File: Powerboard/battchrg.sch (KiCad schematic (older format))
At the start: 48 parts, among them Q1(ACFET)? SI7617DN-T1-GE3

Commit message: 01022022
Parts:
- C14, C6: renamed from C?; value C_Small -> 0.1µF
- C15: renamed from C?; value ? -> 0.1µF
- C16: renamed from C?; value 2.2 μF -> 2.2μF
- C7: renamed from C?; value 1μF -> 1µF
- CTTC: renamed from CTTC?; value CP_Small -> 0.022µF
- L1: renamed from L?; value L -> 6.8µH
- R14, R15: renamed from R?; value R_Small -> 100kΩ
- R17: renamed from R?; value R_Small -> 10Ω
- R18: renamed from R?; value R_Small -> 1kΩ
- R4: renamed from R?; value R -> 150kΩ
- R6: renamed from R?; value R -> 13kΩ
- R8: renamed from R?; value R -> 32kΩ
- RAC: renamed from RAC?; value 0.010 -> 10mΩ
- RSR: renamed from RSR?; value 0.010 -> 10mΩ
- gave numbers to parts that had none: 28
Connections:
- net VDD is gone; now on net System: C15.1, C3.2, C8.1, C9.1, IC?.1 (ACN), Q3.5 (D_1), Q3.6 (D_2), Q3.7 (D_3), Q3.8 (D_4), Q4.5 (D_1), Q4.6 (D_2), Q4.7 (D_3), Q4.8 (D_4), R15.2, RAC.1
- net CE: now also R3.1, R5.1, R7.1, R9.2
- net GND: now also EXTPower.2 (Pin_2), J1.2 (Pin_2)
- net at J1.1 (Pin_1), R10.2, R16.2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: no longer J1.2 (Pin_2)
- net Stat1: now reaches IC?.5 (STAT1)
- net PG: now reaches IC?.8 (~PG)
- net Stat2: now reaches IC?.9 (STAT2)
- net at EXTPower.1 (Pin_1), Q1(ACFET).1 (S_1), Q1(ACFET).2 (S_2)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: no longer EXTPower.2 (Pin_2)
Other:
- moved on the sheet: C15, C4, J1, R15, R9

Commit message: 08/02/2022 update3
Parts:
- added MainPowerDiode: LED, symbol Device:LED
- added MainPowerSwitch: Conn_01x02_Female, symbol Connector:Conn_01x02_Female
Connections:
- net at Q1(ACFET).1 (S_1), Q1(ACFET).2 (S_2), Q1(ACFET).3 (S_3)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: now also MainPowerDiode.1 (K); no longer EXTPower.1 (Pin_1)
- new net: EXTPower.1 (Pin_1), MainPowerSwitch.2 (Pin_2)
- new net: MainPowerDiode.2 (A), MainPowerSwitch.1 (Pin_1)
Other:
- moved on the sheet: C1, C10, C11, C12, C13, C14, C15, C16, C3, C4, C5, C6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

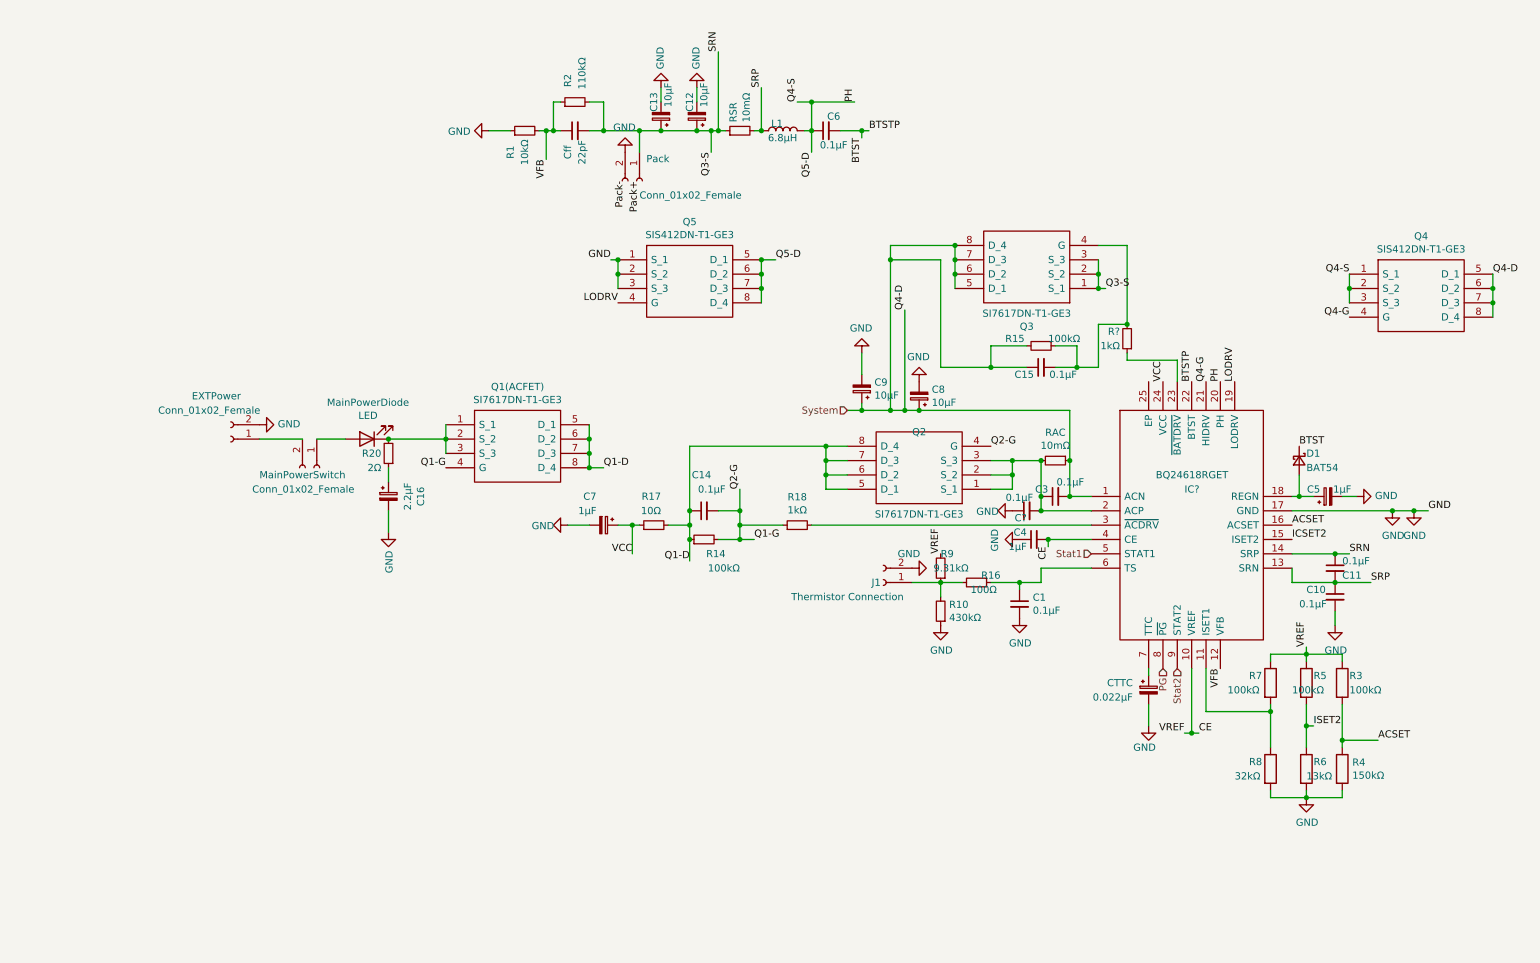
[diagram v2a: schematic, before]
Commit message: reverse polarity protection
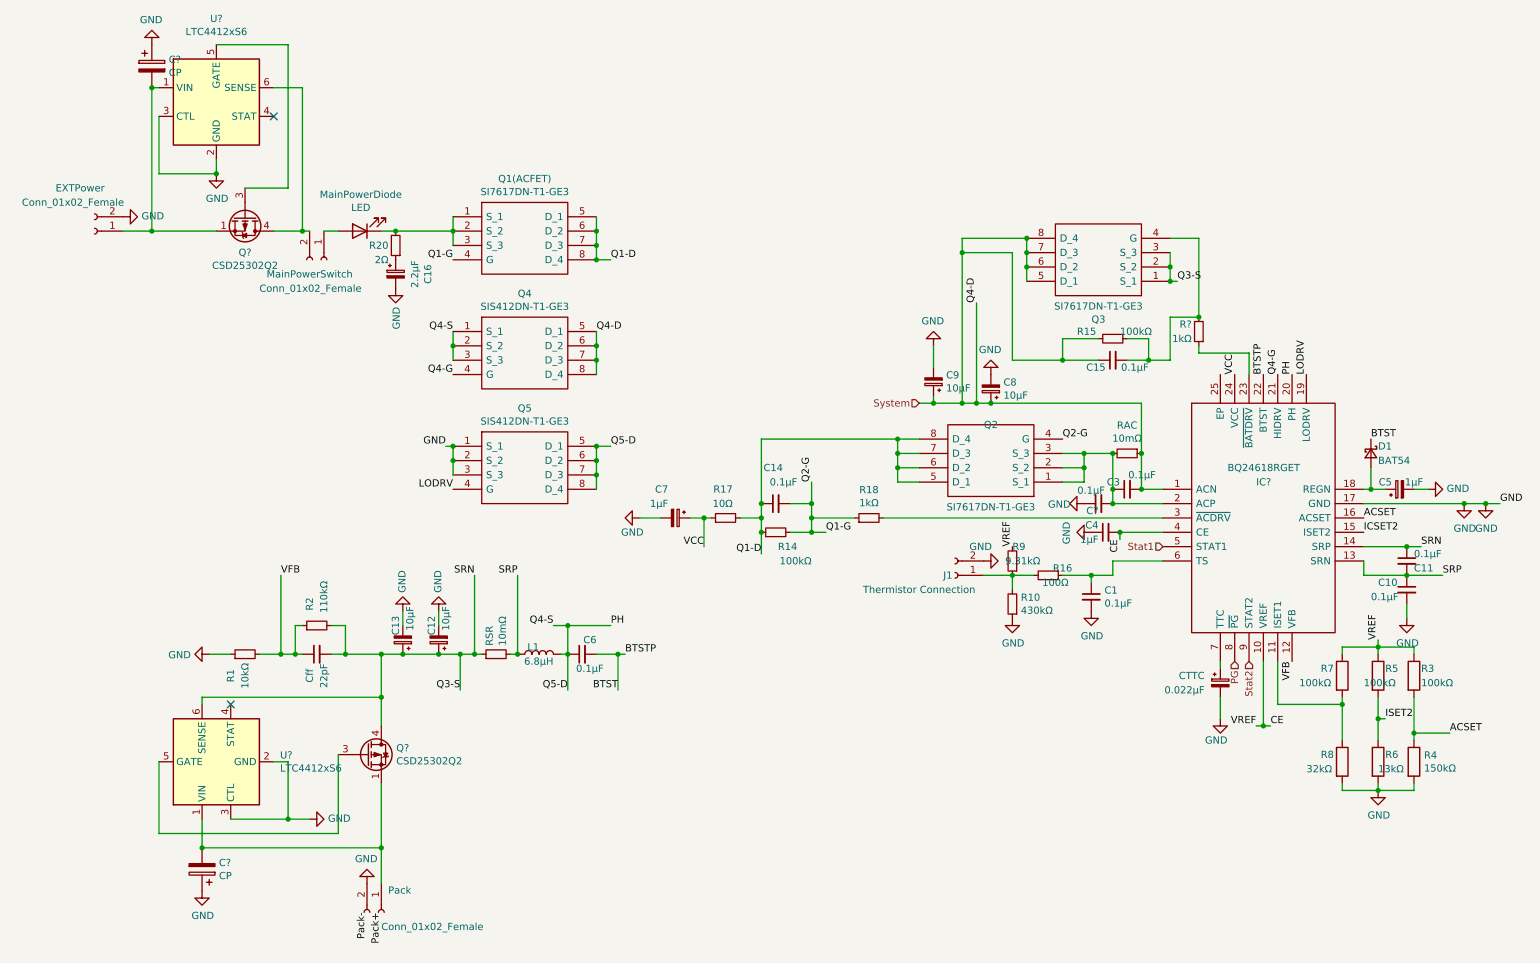
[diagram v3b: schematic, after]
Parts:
- added C? (x2): CP, symbol Device:CP
- added Q? (x2): CSD25302Q2, Package_SON:Texas_DQK, symbol Transistor_FET:CSD25302Q2
- added U? (x2): LTC4412xS6, Package_TO_SOT_SMD:TSOT-23-6, symbol Power_Management:LTC4412xS6
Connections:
- net GND: now also C?.1, C?.1, U?.2 (GND), U?.2 (GND), U?.3 (CTL), U?.3 (CTL)
- net Q3-S: now also Q?.4 (D), Q?.7 (D), U?.6 (SENSE); no longer Pack.1 (Pin_1)
- net at EXTPower.1 (Pin_1): now also C?.2, Q?.1 (S), Q?.2 (S), Q?.5 (S), Q?.6 (S), Q?.8 (S), U?.1 (VIN); no longer MainPowerSwitch.2 (Pin_2)
- new net: C?.2, Pack.1 (Pin_1), Q?.1 (S), Q?.2 (S), Q?.5 (S), Q?.6 (S), Q?.8 (S), U?.1 (VIN)
- new net: Q?.3 (G), U?.5 (GATE) (x2)
- new net: MainPowerSwitch.2 (Pin_2), Q?.4 (D), Q?.7 (D), U?.6 (SENSE)
- no-connect marks 0 -> 2
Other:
- moved on the sheet: C1, C10, C11, C12, C13, C14, C15, C16, C3, C4, C5, C6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

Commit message: 13/02/2022
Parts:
- added TP? (x3): TestPoint, symbol Connector:TestPoint
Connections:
- net System: now also TP?.1
- net at C?.2, EXTPower.1 (Pin_1), Q?.1 (S)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: now also TP?.1
- net at C?.2, Pack.1 (Pin_1), Q?.1 (S)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: now also TP?.1
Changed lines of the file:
@@
 	6650 3050 6650 3200
-Wire Wire Line
-	6550 3450 6650 3450
 Wire Wire Line
 	6650 3400 6650 3450
@@
 Text Label 4450 5450 2    50   ~ 0
 BTST
-Text HLabel 6550 3450 0    50   Input ~ 0
+Text HLabel 6300 3450 0    50   Input ~ 0
 System
 Text HLabel 8850 5250 3    50   Input ~ 0
@@
 Connection ~ 1200 2250
 Wire Wire Line
-	1200 2250 1000 2250
+	1200 2250 1100 2250
 Wire Wire Line
 	1200 2250 1650 2250
@@
 	1750 6350 2150 6350
 Wire Wire Line
-	2800 6550 2800 6800
+	2800 6550 2800 6650
 Connection ~ 2800 6550
 Wire Wire Line
@@
 	0    1    1    0
 $EndComp
+$Comp
+L Connector:TestPoint TP?
+U 1 1 620C3115
+P 1100 2250
+F 0 "TP?" H 1042 2276 50  0000 R CNN
+F 1 "TestPoint" H 1042 2367 50  0000 R CNN
+F 2 "" H 1300 2250 50  0001 C CNN
+F 3 "~" H 1300 2250 50  0001 C CNN
+	1    1100 2250
+	-1   0    0    1
+$EndComp
+Connection ~ 1100 2250
+Wire Wire Line
+	1100 2250 1000 2250
+$Comp
+L Connector:TestPoint TP?
+U 1 1 620C3E08
+P 2800 6650
+F 0 "TP?" V 2754 6838 50  0000 L CNN
+F 1 "TestPoint" V 2845 6838 50  0000 L CNN
+F 2 "" H 3000 6650 50  0001 C CNN
+F 3 "~" H 3000 6650 50  0001 C CNN
+	1    2800 6650
+	0    1    1    0
+$EndComp
+Connection ~ 2800 6650
+Wire Wire Line
+	2800 6650 2800 6800
+Wire Wire Line
+	6300 3450 6450 3450
+$Comp
+L Connector:TestPoint TP?
+U 1 1 620D1148
+P 6450 3450
+F 0 "TP?" H 6508 3568 50  0000 L CNN
+F 1 "TestPoint" H 6508 3477 50  0000 L CNN
+F 2 "" H 6650 3450 50  0001 C CNN
+F 3 "~" H 6650 3450 50  0001 C CNN
+	1    6450 3450
+	1    0    0    -1
+$EndComp
+Connection ~ 6450 3450
+Wire Wire Line
+	6450 3450 6650 3450
 $EndSCHEMATC

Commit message: added lpc/24 enable
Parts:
- IC?: symbol power_new_18122021-rescue:BQ24618RGET-iclr -> power_new_25012022-rescue:BQ24618RGET-iclr-power_new_18122021-rescue
- Q1(ACFET), Q2, Q3: symbol power_new_18122021-rescue:SI7617DN-T1-GE3-iclr -> power_new_25012022-rescue:SI7617DN-T1-GE3-iclr-power_new_18122021-rescue
- Q4, Q5: symbol power_new_18122021-rescue:SIS412DN-T1-GE3-iclr -> power_new_25012022-rescue:SIS412DN-T1-GE3-iclr-power_new_18122021-rescue
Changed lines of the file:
@@
 $EndComp
 $Comp
-L power_new_18122021-rescue:BQ24618RGET-iclr IC?
+L power_new_25012022-rescue:BQ24618RGET-iclr-power_new_18122021-rescue IC?
 U 1 1 61C1BE0B
 P 8250 4050
@@
 $EndComp
 $Comp
-L power_new_18122021-rescue:SI7617DN-T1-GE3-iclr Q?
+L power_new_25012022-rescue:SI7617DN-T1-GE3-iclr-power_new_18122021-rescue Q?
 U 1 1 61C1BEBC
 P 7550 4000
@@
 	3300 2250 3300 2150
 $Comp
-L power_new_18122021-rescue:SI7617DN-T1-GE3-iclr Q1(ACFET)?
+L power_new_25012022-rescue:SI7617DN-T1-GE3-iclr-power_new_18122021-rescue Q1(ACFET)?
 U 1 1 61C1BF64
 P 3300 2150
@@
 	3300 3950 3300 3850
 $Comp
-L power_new_18122021-rescue:SIS412DN-T1-GE3-iclr Q?
+L power_new_25012022-rescue:SIS412DN-T1-GE3-iclr-power_new_18122021-rescue Q?
 U 1 1 61C1BF9B
 P 3300 3750
@@
 Connection ~ 4450 5200
 $Comp
-L power_new_18122021-rescue:SIS412DN-T1-GE3-iclr Q?
+L power_new_25012022-rescue:SIS412DN-T1-GE3-iclr-power_new_18122021-rescue Q?
 U 1 1 61C1BE69
 P 3300 2950
@@
 	6850 2400 7200 2400
 $Comp
-L power_new_18122021-rescue:SI7617DN-T1-GE3-iclr Q?
+L power_new_25012022-rescue:SI7617DN-T1-GE3-iclr-power_new_18122021-rescue Q?
 U 1 1 61C1BEFF
 P 8300 2600

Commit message: 19/02/2022
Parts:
- removed IC?: BQ24618RGET, QFN50P400X400X100-25N-D, symbol power_new_25012022-rescue:BQ24618RGET-iclr-power_new_18122021-rescue
- removed Q1(ACFET), Q2, Q3: SI7617DN-T1-GE3, SIS862DNT1GE3, symbol power_new_25012022-rescue:SI7617DN-T1-GE3-iclr-power_new_18122021-rescue
- removed Q4, Q5: SIS412DN-T1-GE3, POWERPAK-1212-8, symbol power_new_25012022-rescue:SIS412DN-T1-GE3-iclr-power_new_18122021-rescue
- added IC?: BQ24618RGET-iclr, QFN50P400X400X100-25N-D, symbol iclr:BQ24618RGET-iclr
- added Q1, Q2, Q3: SI7617DN-T1-GE3, SIS862DNT1GE3, symbol iclr:SI7617DN-T1-GE3
- added Q4, Q5: SIS412DN-T1-GE3-iclr, POWERPAK-1212-8, symbol iclr:SIS412DN-T1-GE3-iclr
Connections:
- net ACSET: now also IC?.16 (ACSET)
- net BTST: now also IC?.22 (BTST)
- net CE: now also IC?.10 (VREF), IC?.4 (CE)
- net GND: now also IC?.17 (GND), Q5.1 (S_1), Q5.2 (S_2), Q5.3 (S_3)
- net ICSET2: now also IC?.15 (ISET2)
- net LODRV: now also IC?.19 (LODRV), Q5.4 (G)
- net PG: now also IC?.8 (~PG)
- net PH: now also IC?.20 (PH), Q4.1 (S_1), Q4.2 (S_2), Q4.3 (S_3), Q5.5 (D_1), Q5.6 (D_2), Q5.7 (D_3), Q5.8 (D_4)
- net Q1-D: now also Q1.5 (D_1), Q1.6 (D_2), Q1.7 (D_3), Q1.8 (D_4), Q2.5 (D_1), Q2.6 (D_2), Q2.7 (D_3), Q2.8 (D_4)
- net Q1-G: now also Q1.4 (G), Q2.4 (G)
- net Q3-S: now also IC?.14 (SRP), Q3.1 (S_1), Q3.2 (S_2), Q3.3 (S_3)
- net Q4-G: now also IC?.21 (HIDRV), Q4.4 (G)
- net SRP: now also IC?.13 (SRN)
- net Stat1: now also IC?.5 (STAT1)
- net Stat2: now also IC?.9 (STAT2)
- net System: now also IC?.1 (ACN), Q3.5 (D_1), Q3.6 (D_2), Q3.7 (D_3), Q3.8 (D_4), Q4.5 (D_1), Q4.6 (D_2), Q4.7 (D_3), Q4.8 (D_4)
- net VCC: now also IC?.24 (VCC)
- net VFB: now also IC?.12 (VFB)
- net at C3.1, C?.2, RAC.2: now also IC?.2 (ACP), Q2.1 (S_1), Q2.2 (S_2), Q2.3 (S_3)
- net at C1.1, R16.1: now also IC?.6 (TS)
- net at R7.2, R8.1: now also IC?.11 (ISET1)
- net at C5.1, D1.2 (A): now also IC?.18 (REGN)
- net at R?.1: now also IC?.23 (~BATDRV)
- net at R18.2: now also IC?.3 (~ACDRV)
- net at CTTC.1: now also IC?.7 (TTC)
- net at C15.2, R15.1, R?.2: now also Q3.4 (G)
- net at MainPowerDiode.1 (K), R20.2: now also Q1.1 (S_1), Q1.2 (S_2), Q1.3 (S_3)
